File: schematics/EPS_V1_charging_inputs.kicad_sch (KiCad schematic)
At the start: 27 parts, among them U4 MP28167GQ-Z, U7 TPS2121RUXR

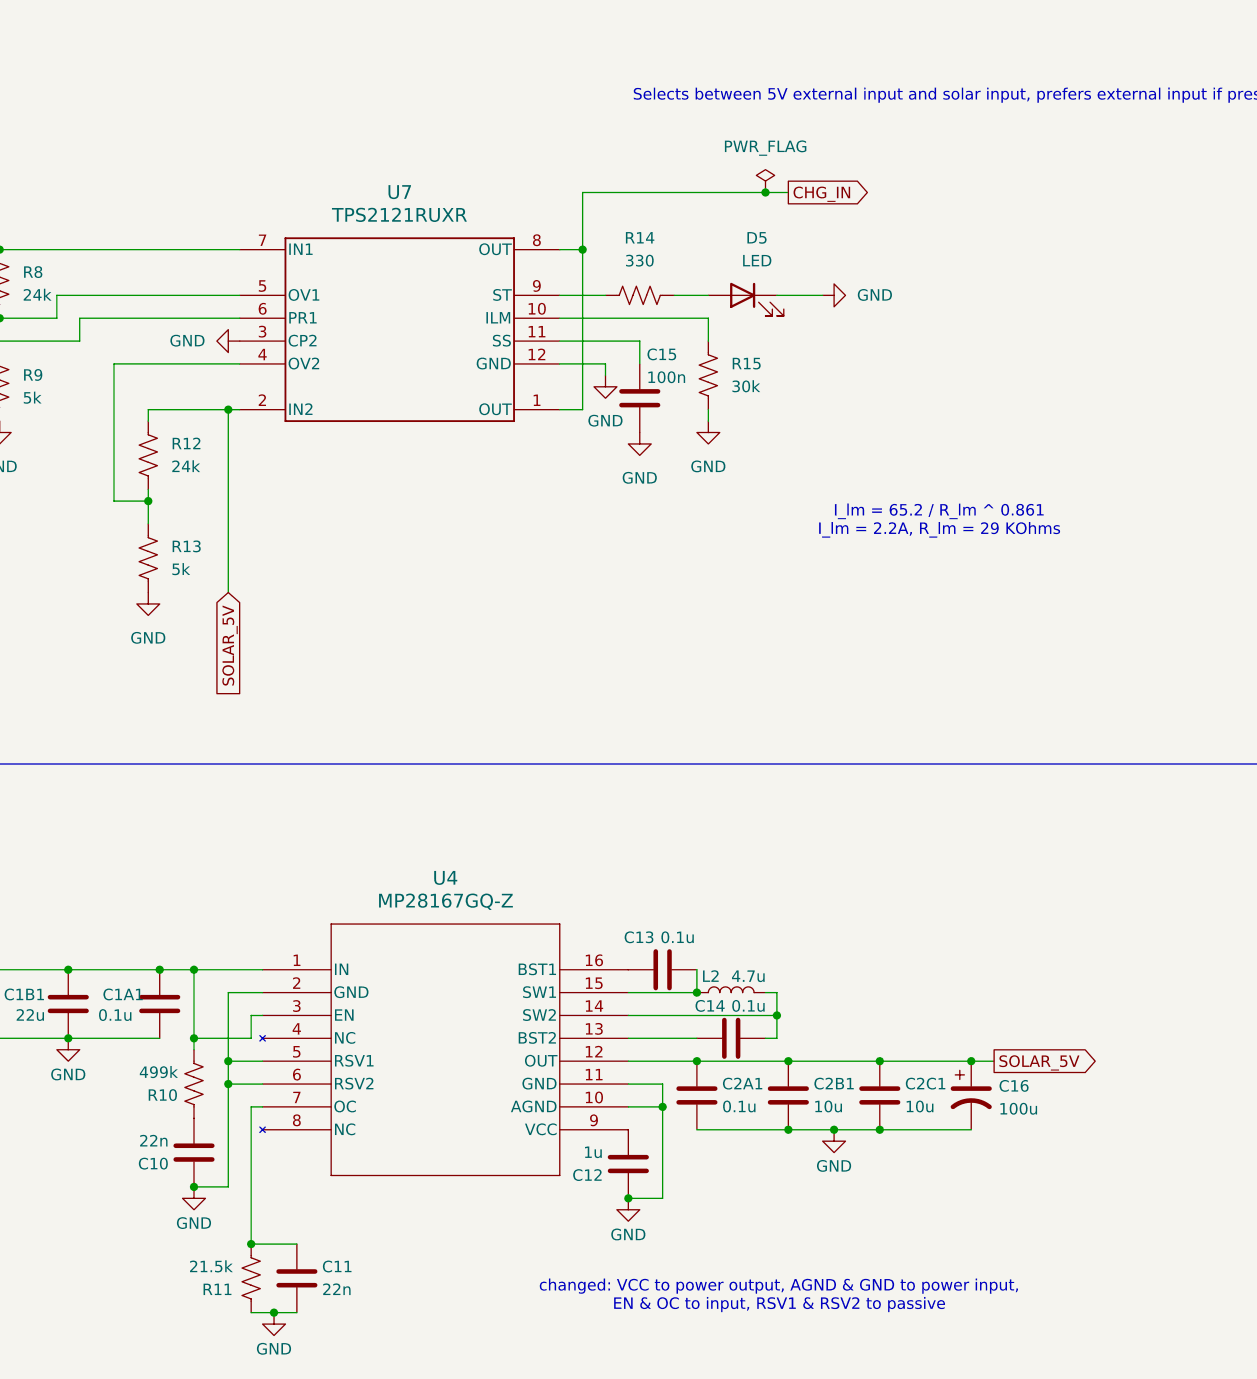
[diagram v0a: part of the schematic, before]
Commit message: Fix NC pins, add 2 test points & silkscreen labels
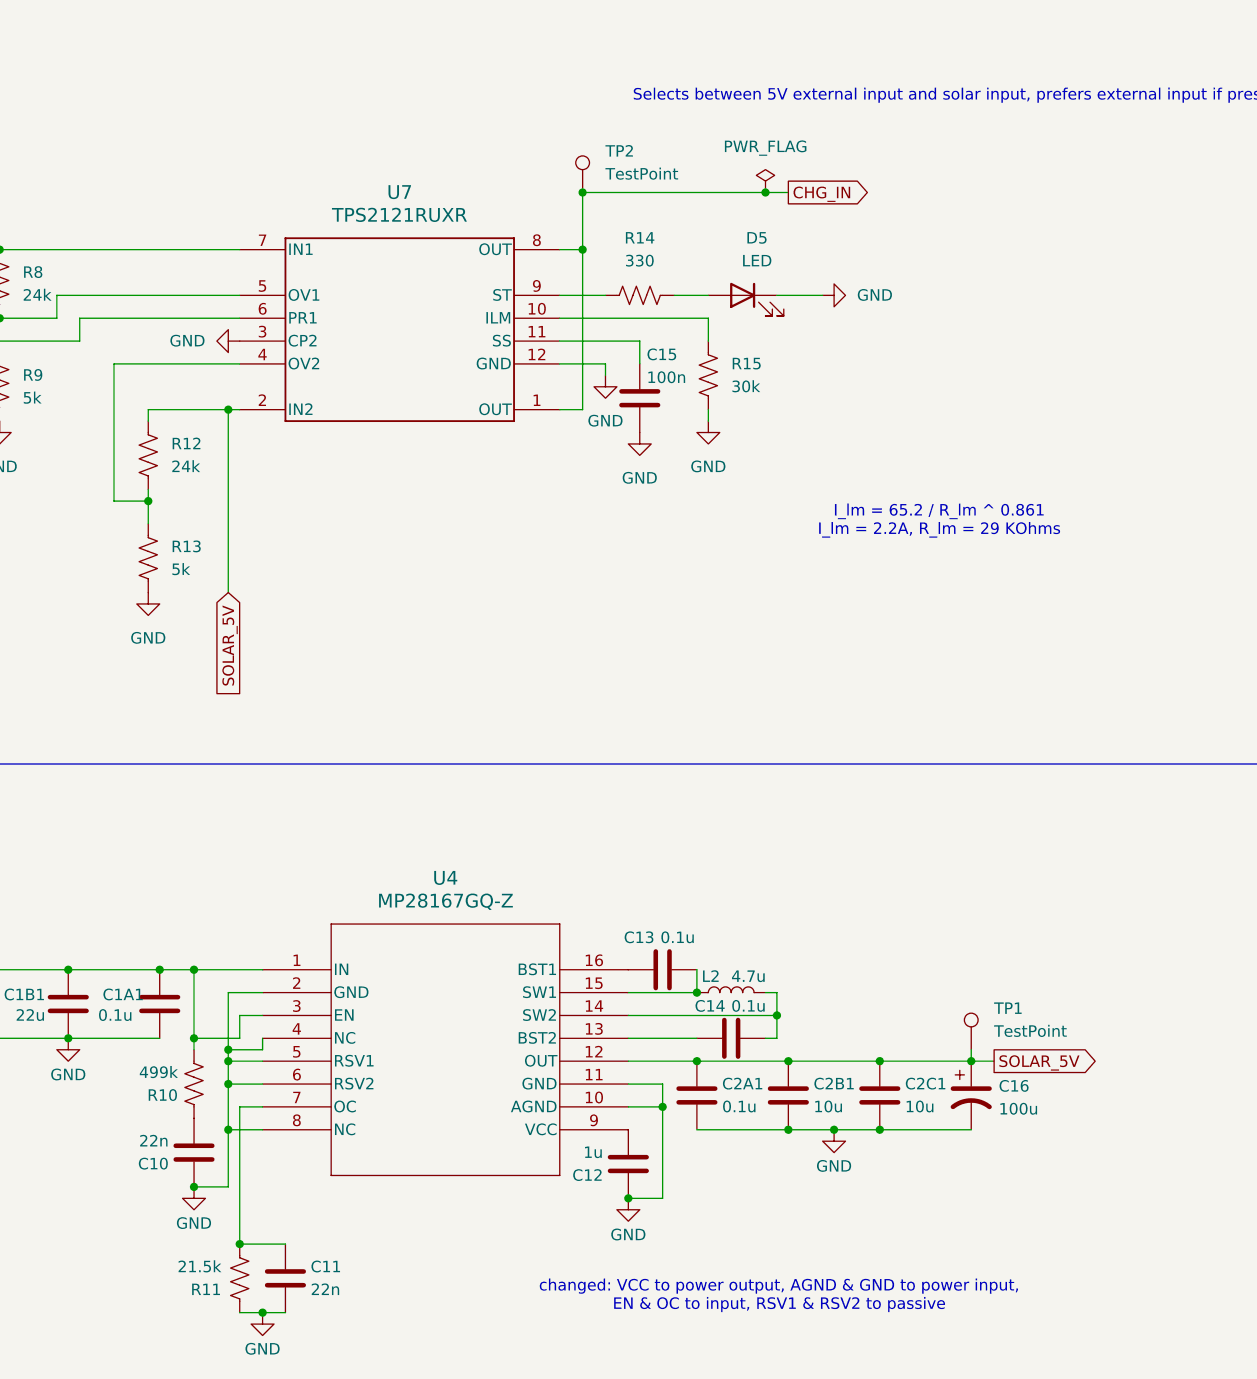
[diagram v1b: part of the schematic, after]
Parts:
- added TP1, TP2: TestPoint, TestPoint:TestPoint_Pad_D1.5mm, symbol Connector:TestPoint
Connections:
- net CHG_IN: now also TP2.1
- net GND: now also U4.4 (NC), U4.8 (NC)
- net SOLAR_5V: now also TP1.1
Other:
- moved on the sheet: C11, R11

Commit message: Fix silkscreen; Fix component value style
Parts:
- C13, C14, C1A1, C2A1: value 0.1u -> 100n
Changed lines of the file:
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@@
 			)
 		)
-		(property "Value" "0.1u"
+		(property "Value" "100n"
 			(at 169.164 135.89 0)
 			(show_name no)
@@
 			)
 		)
-		(property "Value" "0.1u"
+		(property "Value" "100n"
 			(at 170.18 124.714 90)
 			(show_name no)
@@
 			)
 		)
-		(property "Value" "0.1u"
+		(property "Value" "100n"
 			(at 99.822 125.73 0)
 			(show_name no)
@@
 			)
 		)
-		(property "Value" "0.1u"
+		(property "Value" "100n"
 			(at 162.306 117.094 90)
 			(show_name no)

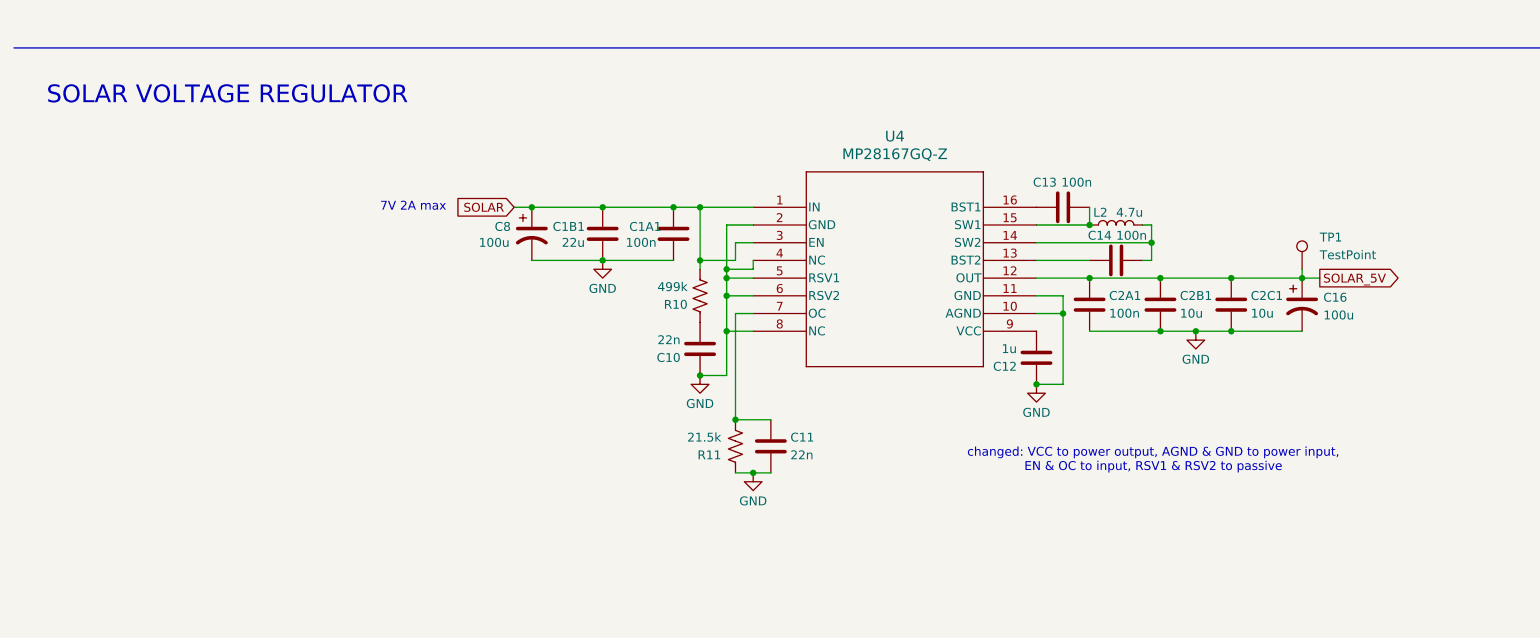
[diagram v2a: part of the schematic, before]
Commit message: Switch out MP28167 for LTC3119 (MPPC buck-boost) in schematic
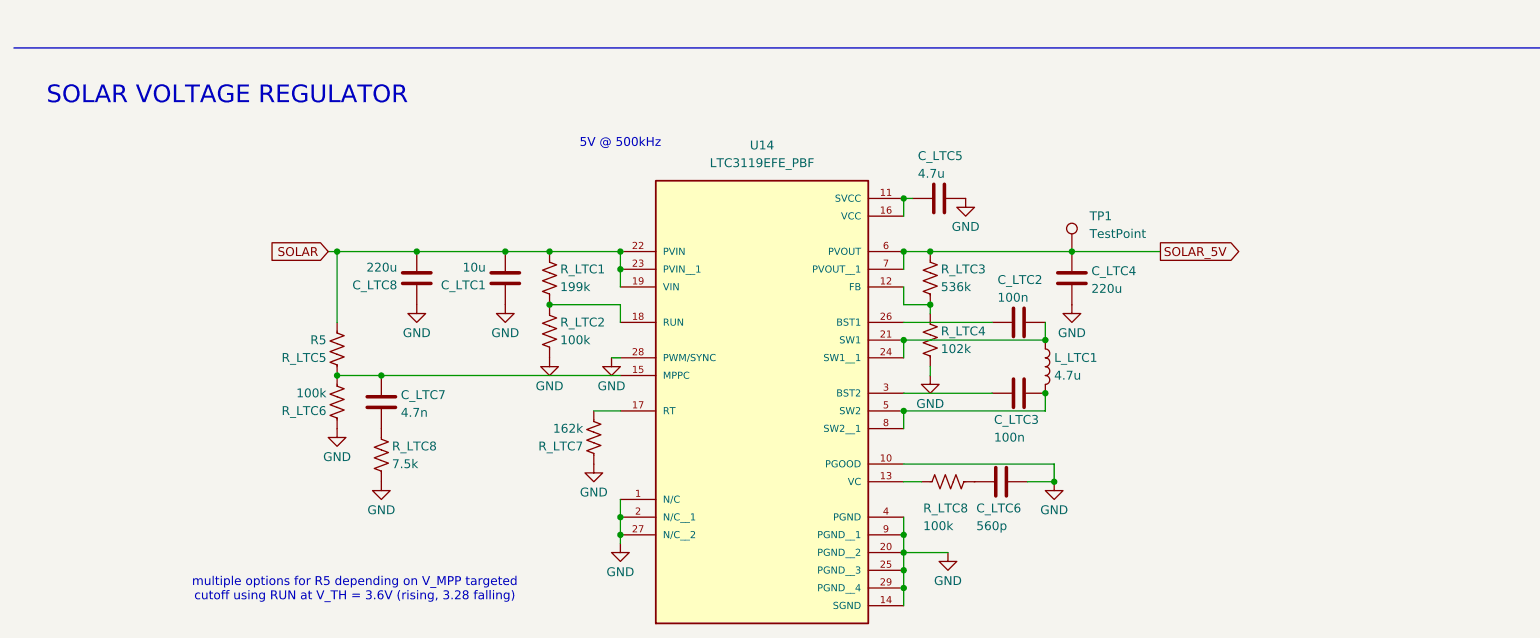
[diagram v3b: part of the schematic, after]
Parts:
- removed C10, C11: 22n, Capacitor_SMD:C_0603_1608Metric, symbol Device:C
- removed C12: 1u, Capacitor_SMD:C_0603_1608Metric, symbol Device:C
- removed C13, C14, C1A1, C2A1: 100n, Capacitor_SMD:C_0603_1608Metric, symbol Device:C
- removed C16, C8: 100u, Capacitor_SMD:CP_Elec_6.3x5.4, symbol Device:C_Polarized_US
- removed C1B1: 22u, Capacitor_SMD:C_0805_2012Metric, symbol Device:C
- removed C2B1, C2C1: 10u, Capacitor_SMD:C_0805_2012Metric, symbol Device:C
- removed L2: 4.7u, footprints:IND_ASPI-7318-4R7M-T, symbol Device:L
- removed R10: 499k, Resistor_SMD:R_0603_1608Metric, symbol Device:R_US
- removed R11: 21.5k, Resistor_SMD:R_0603_1608Metric, symbol Device:R_US
- removed U4: MP28167GQ-Z, footprints:QFN-16_MP28167GQ_MNP, symbol MP28167GQ-Z:MP28167GQ-Z
- added C_LTC1: 10u, symbol Device:C
- added C_LTC2, C_LTC3: 100n, symbol Device:C
- added C_LTC4, C_LTC8: 220u, symbol Device:C
- added C_LTC5: 4.7u, symbol Device:C
- added C_LTC6: 560p, symbol Device:C
- added C_LTC7: 4.7n, symbol Device:C
- added L_LTC1: 4.7u, symbol Device:L
- added R_LTC1: 199k, symbol Device:R_US
- added R_LTC2, R_LTC6, R_LTC8: 100k, symbol Device:R_US
- added R_LTC3: 536k, symbol Device:R_US
- added R_LTC4: 102k, symbol Device:R_US
- added R_LTC5: R5, symbol Device:R_US
- added R_LTC7: 162k, symbol Device:R_US
- added R_LTC8: 7.5k, symbol Device:R_US
- added U14: LTC3119EFE_PBF, LTC3119EFE_PBF:SOP65P640X120-29N, symbol LTC3119EFE_PBF:LTC3119EFE_PBF
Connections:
- net GND: now also C_LTC1.2, C_LTC4.1, C_LTC5.1, C_LTC6.1, C_LTC8.2, R_LTC2.2, R_LTC4.2, R_LTC6.1, R_LTC7.1, R_LTC8.2, U14.1 (N/C), U14.10 (PGOOD), U14.14 (SGND), U14.2 (N/C__1), U14.20 (PGND__2), U14.25 (PGND__3), U14.27 (N/C__2), U14.28 (PWM/SYNC), U14.29 (PGND__4), U14.4 (PGND), U14.9 (PGND__1)
- net SOLAR: now also C_LTC1.1, C_LTC8.1, R_LTC1.1, R_LTC5.2, U14.19 (VIN), U14.22 (PVIN), U14.23 (PVIN__1)
- net SOLAR_5V: now also C_LTC4.2, R_LTC3.1, U14.6 (PVOUT), U14.7 (PVOUT__1)
- new net: C_LTC2.1, L_LTC1.1, U14.21 (SW1), U14.24 (SW1__1)
- new net: C_LTC3.1, L_LTC1.2, U14.5 (SW2), U14.8 (SW2__1)
- new net: C_LTC5.2, U14.11 (SVCC), U14.16 (VCC)
- new net: R_LTC3.2, R_LTC4.1, U14.12 (FB)
- new net: R_LTC8.1, U14.13 (VC)
- new net: C_LTC7.2, R_LTC5.1, R_LTC6.2, U14.15 (MPPC)
- new net: R_LTC7.2, U14.17 (RT)
- new net: R_LTC1.2, R_LTC2.1, U14.18 (RUN)
- new net: C_LTC2.2, U14.26 (BST1)
- new net: C_LTC3.2, U14.3 (BST2)
- new net: C_LTC6.2, R_LTC8.2
- new net: C_LTC7.1, R_LTC8.1
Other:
- note added: "5V @ 500kHz"
- note added: "multiple options for R5 depending on V_MPP targeted cutoff using RUN at V_TH = 3.6V (rising, 3.28 falling)"
- note removed: "7V 2A max"
- note removed: "changed: VCC to power output, AGND & GND to power input, EN & OC to input, RSV1 & RSV2 to passive"

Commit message: Rename some resistors
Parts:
- renumbered R_LTC8 to R_LTC7, R_LTC7 to R_LTC8, R_LTC8 to R_LTC9
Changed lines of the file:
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@@
 		(in_pos_files yes)
 		(dnp no)
-		(property "Reference" "R_LTC8"
+		(property "Reference" "R_LTC9"
 			(at 142.494 163.83 90)
 			(show_name no)
@@
 			(project "EPS_V1"
 				(path "/85157432-5d03-48fa-ab40-27ed3d133f47/200409e9-92e5-48dc-b89e-cefaee3c74ba"
-					(reference "R_LTC8")
+					(reference "R_LTC9")
 					(unit 1)
 				)
@@
 		(in_pos_files yes)
 		(dnp no)
-		(property "Reference" "R_LTC8"
+		(property "Reference" "R_LTC7"
 			(at 66.294 154.94 0)
 			(show_name no)
@@
 			(project "EPS_V1"
 				(path "/85157432-5d03-48fa-ab40-27ed3d133f47/200409e9-92e5-48dc-b89e-cefaee3c74ba"
-					(reference "R_LTC8")
+					(reference "R_LTC7")
 					(unit 1)
 				)
@@
 		(in_pos_files yes)
 		(dnp no)
-		(property "Reference" "R_LTC7"
+		(property "Reference" "R_LTC8"
 			(at 93.726 154.94 0)
 			(show_name no)
@@
 			(project "EPS_V1"
 				(path "/85157432-5d03-48fa-ab40-27ed3d133f47/200409e9-92e5-48dc-b89e-cefaee3c74ba"
-					(reference "R_LTC7")
-					(unit 1)
-				)
+					(reference "R_LTC8")
+					(unit 1)
+				)

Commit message: Do layout with new regulator
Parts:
- removed C_LTC8: 220u, symbol Device:C
- added C_LTC10: 10u, Capacitor_SMD:C_0805_2012Metric, symbol Device:C
- added C_LTC4: 220u, footprints:CAPMP7.6X4.3_4.3N_KEM, symbol Device:C
- added C_LTC9: 100u, Capacitor_SMD:C_1210_3225Metric, symbol Device:C
- added NT11: NetTie_2, NetTie:NetTie-2_SMD_Pad0.5mm, symbol Device:NetTie_2
- added R_LTC10: 0.33R, Resistor_SMD:R_0603_1608Metric, symbol Device:R_US
- C_LTC1: footprint (none) -> Capacitor_SMD:C_0805_2012Metric
- C_LTC2, C_LTC3, C_LTC5, C_LTC6, C_LTC7: footprint (none) -> Capacitor_SMD:C_0603_1608Metric
- C_LTC8: renamed from C_LTC4; value 220u -> 100u; footprint (none) -> Capacitor_SMD:C_1210_3225Metric
- L_LTC1: footprint (none) -> footprints:IND_ASPI-7318-4R7M-T
- R_LTC1, R_LTC2, R_LTC3, R_LTC4, R_LTC5, R_LTC6, R_LTC7, R_LTC8, R_LTC9: footprint (none) -> Resistor_SMD:R_0603_1608Metric
- U14: footprint LTC3119EFE_PBF:SOP65P640X120-29N -> footprints:SOP65P640X120-29N
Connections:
- net GND: now also C_LTC4.2, C_LTC9.1, NT11.2, R_LTC10.1; no longer R_LTC4.2, R_LTC8.1, U14.14 (SGND)
- net SOLAR: now also C_LTC10.1, C_LTC4.1
- net SOLAR_5V: now also C_LTC9.2
- new net: C_LTC10.2, R_LTC10.2
- new net GNDS: NT11.1, R_LTC4.2, R_LTC8.1, U14.14 (SGND)
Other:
- moved on the sheet: C_LTC7, R_LTC5, R_LTC6, R_LTC7, TP1
